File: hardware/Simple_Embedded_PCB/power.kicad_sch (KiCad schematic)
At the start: 34 parts, among them J7 5.5mm X 2.1mm Jack, Q2 AO3401A, U2 LMR16020PDDA, U3 AMS1117-3.3

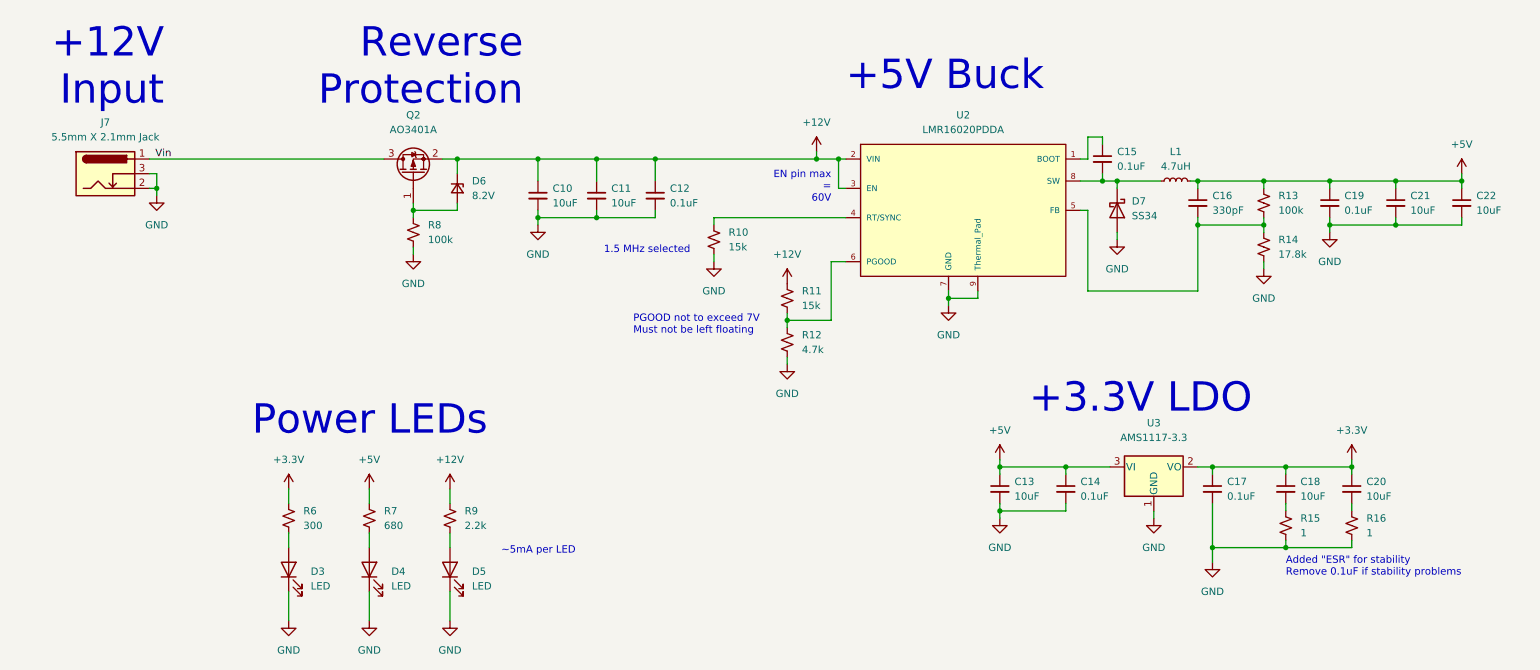
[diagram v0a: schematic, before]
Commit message: Added 4.7k pullups to I2C and reannotated
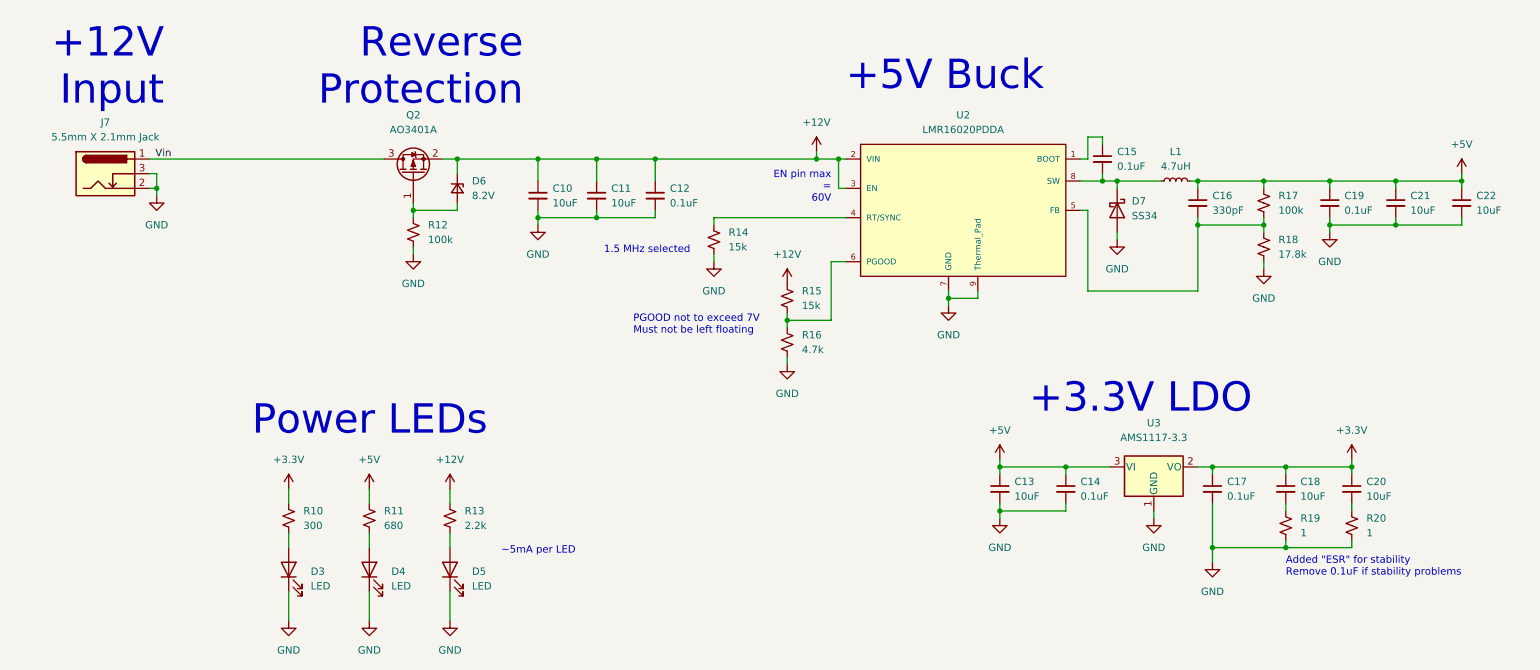
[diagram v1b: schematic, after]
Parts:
- renumbered R6 to R10, R7 to R11, R8 to R12, R9 to R13, R10 to R14, R11 to R15, R12 to R16, R13 to R17, R14 to R18, R15 to R19, R16 to R20
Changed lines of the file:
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@@
   (symbol (lib_id "Device:R_Small_US") (at 144.78 78.74 180) (unit 1)
     (in_bom yes) (on_board yes) (fields_autoplaced)
-    (property "Reference" "R12" (id 0) (at 147.32 77.4699 0)
+    (property "Reference" "R16" (id 0) (at 147.32 77.4699 0)
       (effects (font (size 1.27 1.27)) (justify right))
     )
@@
   (symbol (lib_id "Device:R_Small_US") (at 86.36 109.22 180) (unit 1)
     (in_bom yes) (on_board yes) (fields_autoplaced)
-    (property "Reference" "R9" (id 0) (at 88.9 107.9499 0)
+    (property "Reference" "R13" (id 0) (at 88.9 107.9499 0)
       (effects (font (size 1.27 1.27)) (justify right))
     )
@@
   (symbol (lib_id "Device:R_Small_US") (at 242.57 110.49 180) (unit 1)
     (in_bom yes) (on_board yes) (fields_autoplaced)
-    (property "Reference" "R16" (id 0) (at 245.11 109.2199 0)
+    (property "Reference" "R20" (id 0) (at 245.11 109.2199 0)
       (effects (font (size 1.27 1.27)) (justify right))
     )
@@
   (symbol (lib_id "Device:R_Small_US") (at 227.33 62.23 180) (unit 1)
     (in_bom yes) (on_board yes) (fields_autoplaced)
-    (property "Reference" "R14" (id 0) (at 229.87 60.9599 0)
+    (property "Reference" "R18" (id 0) (at 229.87 60.9599 0)
       (effects (font (size 1.27 1.27)) (justify right))
     )
@@
   (symbol (lib_id "Device:R_Small_US") (at 144.78 71.12 180) (unit 1)
     (in_bom yes) (on_board yes) (fields_autoplaced)
-    (property "Reference" "R11" (id 0) (at 147.32 69.8499 0)
+    (property "Reference" "R15" (id 0) (at 147.32 69.8499 0)
       (effects (font (size 1.27 1.27)) (justify right))
     )
@@
   (symbol (lib_id "Device:R_Small_US") (at 227.33 54.61 180) (unit 1)
     (in_bom yes) (on_board yes) (fields_autoplaced)
-    (property "Reference" "R13" (id 0) (at 229.87 53.3399 0)
+    (property "Reference" "R17" (id 0) (at 229.87 53.3399 0)
       (effects (font (size 1.27 1.27)) (justify right))
     )
@@
   (symbol (lib_id "Device:R_Small_US") (at 72.39 109.22 180) (unit 1)
     (in_bom yes) (on_board yes) (fields_autoplaced)
-    (property "Reference" "R7" (id 0) (at 74.93 107.9499 0)
+    (property "Reference" "R11" (id 0) (at 74.93 107.9499 0)
       (effects (font (size 1.27 1.27)) (justify right))
     )
@@
   (symbol (lib_id "Device:R_Small_US") (at 132.08 60.96 180) (unit 1)
     (in_bom yes) (on_board yes) (fields_autoplaced)
-    (property "Reference" "R10" (id 0) (at 134.62 59.6899 0)
+    (property "Reference" "R14" (id 0) (at 134.62 59.6899 0)
       (effects (font (size 1.27 1.27)) (justify right))
     )
@@
   (symbol (lib_id "Device:R_Small_US") (at 231.14 110.49 180) (unit 1)
     (in_bom yes) (on_board yes) (fields_autoplaced)
-    (property "Reference" "R15" (id 0) (at 233.68 109.2199 0)
+    (property "Reference" "R19" (id 0) (at 233.68 109.2199 0)
       (effects (font (size 1.27 1.27)) (justify right))
     )
@@
   (symbol (lib_id "Device:R_Small_US") (at 58.42 109.22 180) (unit 1)
     (in_bom yes) (on_board yes) (fields_autoplaced)
-    (property "Reference" "R6" (id 0) (at 60.96 107.9499 0)
+    (property "Reference" "R10" (id 0) (at 60.96 107.9499 0)
       (effects (font (size 1.27 1.27)) (justify right))
     )
@@
   (symbol (lib_id "Device:R_Small_US") (at 80.01 59.69 0) (unit 1)
     (in_bom yes) (on_board yes) (fields_autoplaced)
-    (property "Reference" "R8" (id 0) (at 82.55 58.4199 0)
-      (effects (font (size 1.27 1.27)) (justify left))
-    )
+    (property "Reference" "R12" (id 0) (at 82.55 58.4199 0)
+      (effects (font (size 1.27 1.27)) (justify left))
+    )

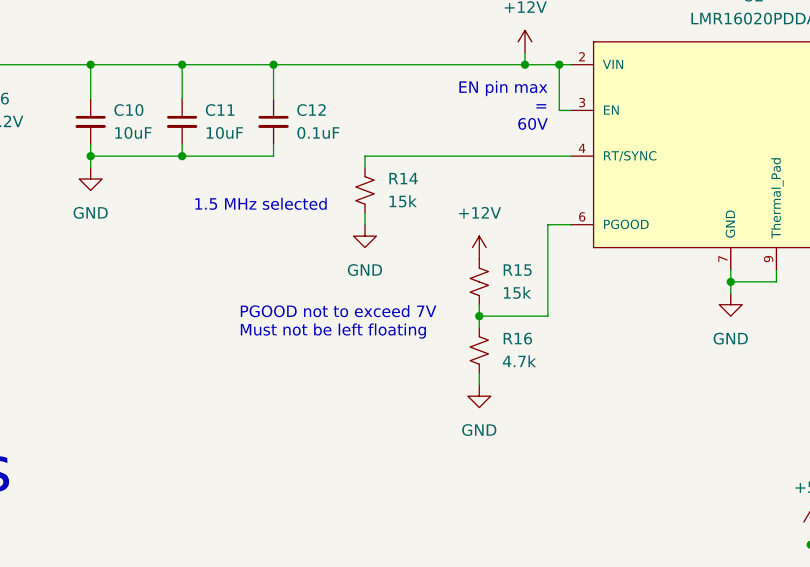
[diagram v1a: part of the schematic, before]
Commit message: Removed comment regarding PGOOD floating, changed PGOOD PU resistor
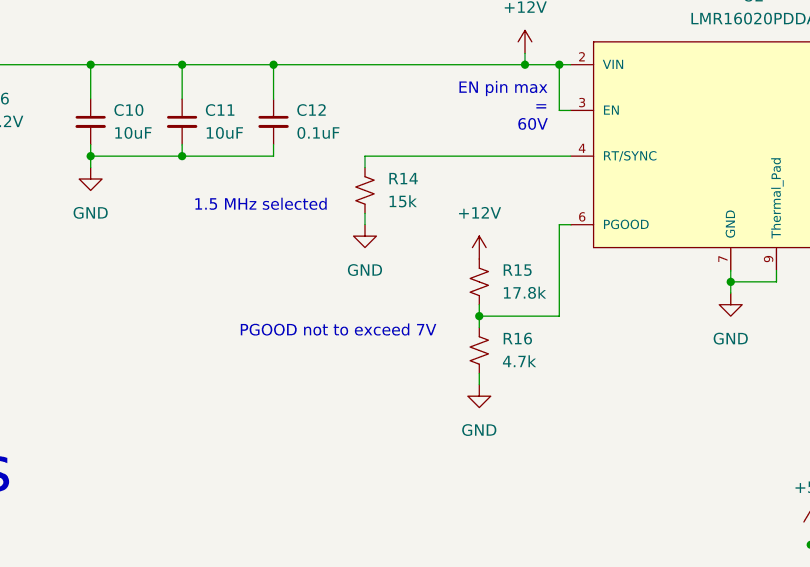
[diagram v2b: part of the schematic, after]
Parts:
- R15: value 15k -> 17.8k
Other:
- note added: "PGOOD not to exceed 7V"
- note removed: "PGOOD not to exceed 7V Must not be left floating"
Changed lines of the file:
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@@
   (title_block
     (title "Power")
-    (date "2022-10-19")
+    (date "2022-10-20")
     (company "Oregon State University")
     (comment 1 "Author: Austin Goergen")
@@
     (stroke (width 0) (type default) (color 0 0 0 0))
   )
-  (wire (pts (xy 152.4 64.77) (xy 154.94 64.77))
+  (wire (pts (xy 153.67 64.77) (xy 154.94 64.77))
     (stroke (width 0) (type default) (color 0 0 0 0))
   )
@@
     (stroke (width 0) (type default) (color 0 0 0 0))
   )
-  (wire (pts (xy 152.4 64.77) (xy 152.4 74.93))
+  (wire (pts (xy 153.67 64.77) (xy 153.67 74.93))
     (stroke (width 0) (type default) (color 0 0 0 0))
   )
@@
     (stroke (width 0) (type default) (color 0 0 0 0))
   )
-  (wire (pts (xy 144.78 74.93) (xy 152.4 74.93))
+  (wire (pts (xy 144.78 74.93) (xy 153.67 74.93))
     (stroke (width 0) (type default) (color 0 0 0 0))
   )
@@
     (effects (font (size 1.27 1.27)) (justify left bottom))
   )
-  (text "PGOOD not to exceed 7V\nMust not be left floating" (at 118.11 77.47 0)
+  (text "PGOOD not to exceed 7V" (at 118.11 77.47 0)
     (effects (font (size 1.27 1.27)) (justify left bottom))
   )
@@
   )
   (symbol (lib_id "Device:R_Small_US") (at 144.78 71.12 180) (unit 1)
-    (in_bom yes) (on_board yes) (fields_autoplaced)
+    (in_bom yes) (on_board yes)
     (property "Reference" "R15" (id 0) (at 147.32 69.8499 0)
       (effects (font (size 1.27 1.27)) (justify right))
     )
-    (property "Value" "15k" (id 1) (at 147.32 72.3899 0)
-      (effects (font (size 1.27 1.27)) (justify right))
-    )
+    (property "Value" "17.8k" (id 1) (at 147.32 72.3899 0)
+      (effects (font (size 1.27 1.27)) (justify right))
+    )

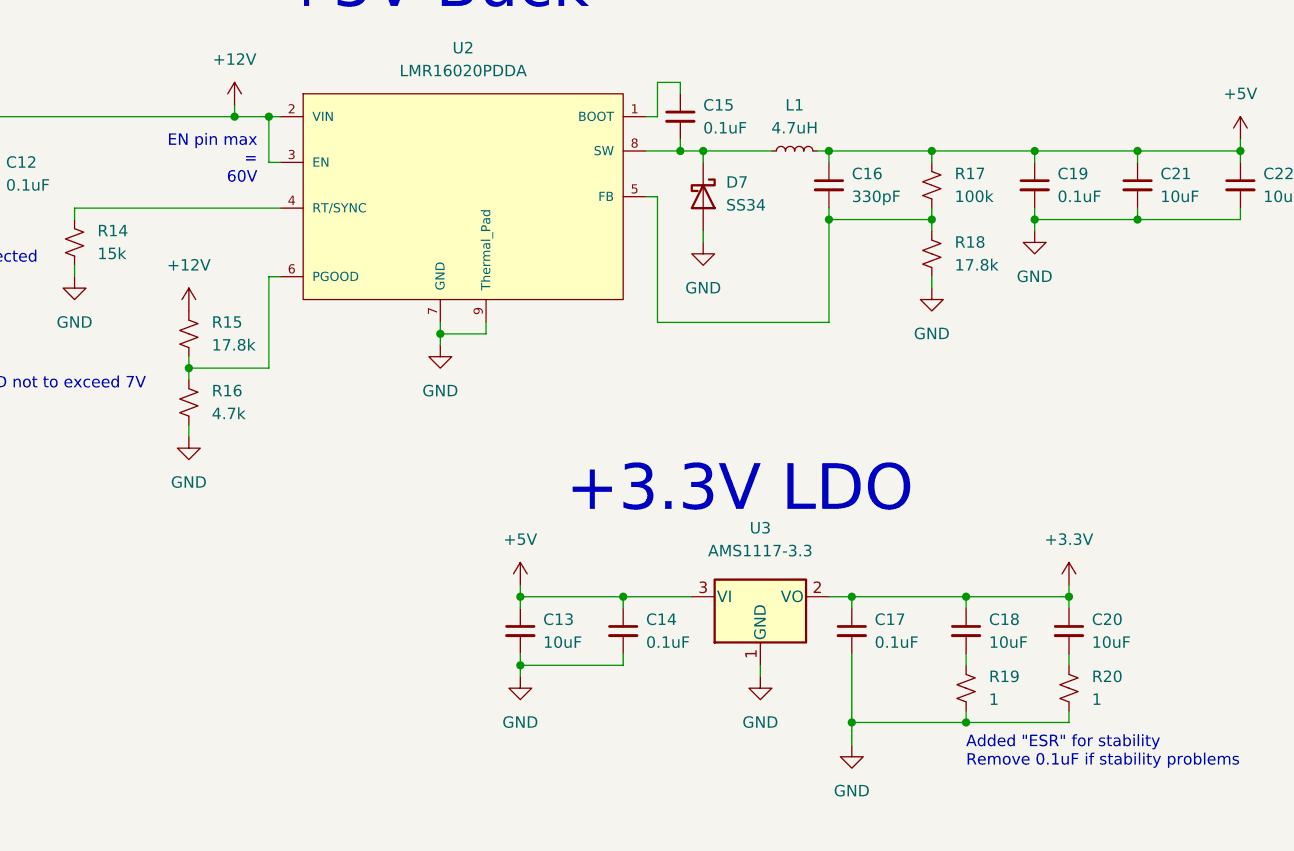
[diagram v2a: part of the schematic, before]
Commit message: Preliminary layout done, removed resistors from PGOOD to just leave it floating
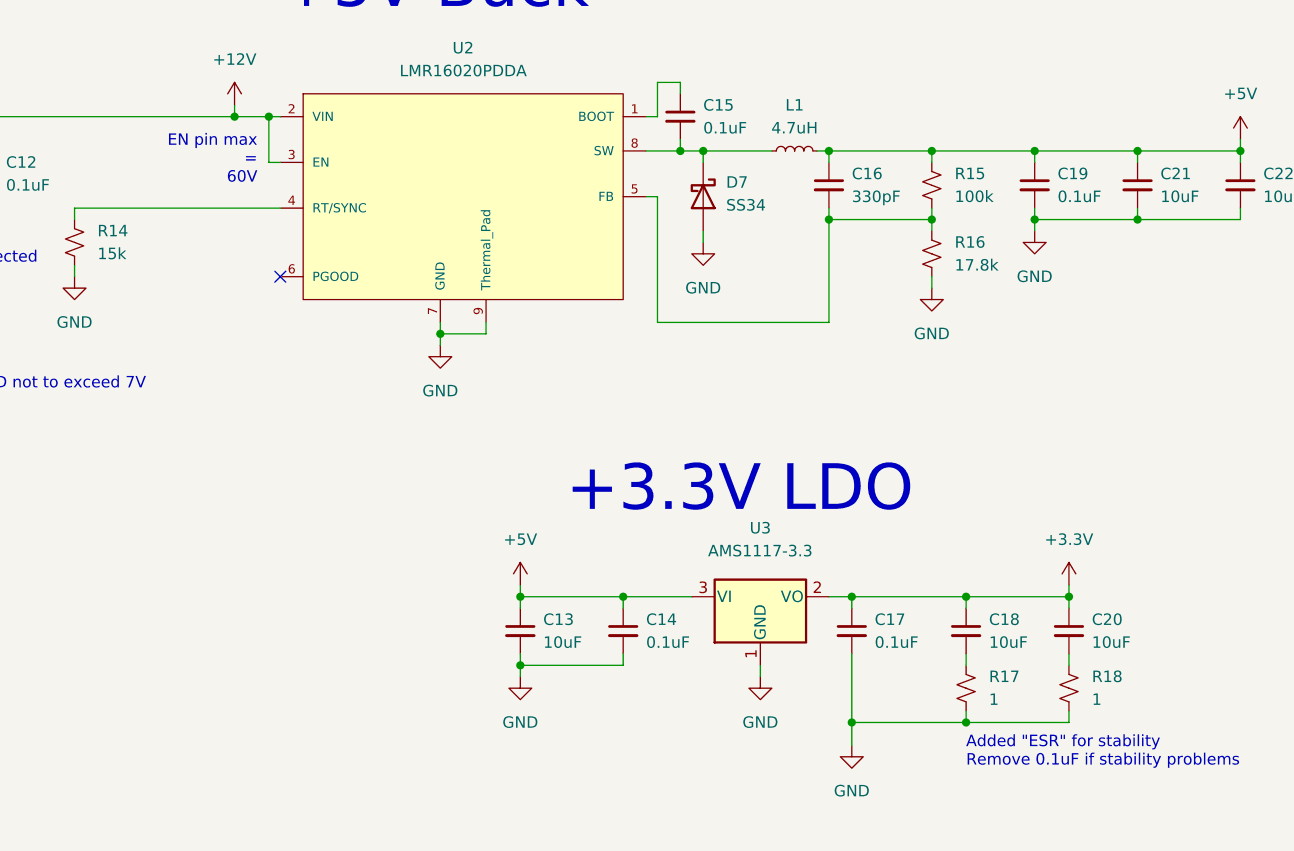
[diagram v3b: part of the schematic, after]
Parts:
- removed R15: 17.8k, symbol Device:R_Small_US
- removed R16: 4.7k, symbol Device:R_Small_US
- C10, C11, C18, C20, C21, C22: footprint (none) -> Capacitor_SMD:C_1206_3216Metric
- C12: footprint (none) -> Capacitor_SMD:C_0603_1608Metric
- C13: footprint (none) -> Capacitor_SMD:C_0805_2012Metric
- C14, C15, C16, C17, C19: footprint (none) -> Capacitor_SMD:C_0402_1005Metric
- D6: footprint (none) -> Diode_SMD:D_SOD-123
- R10, R11, R12, R13: footprint (none) -> Resistor_SMD:R_0603_1608Metric
- R14: footprint (none) -> Resistor_SMD:R_0402_1005Metric
- R15: renamed from R17; footprint (none) -> Resistor_SMD:R_0402_1005Metric
- R16: renamed from R18; footprint (none) -> Resistor_SMD:R_0402_1005Metric
- R17: renamed from R19; footprint (none) -> Resistor_SMD:R_0603_1608Metric
- R18: renamed from R20; footprint (none) -> Resistor_SMD:R_0603_1608Metric
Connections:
- no-connect marks 0 -> 1
